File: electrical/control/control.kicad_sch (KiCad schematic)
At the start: 46 parts, among them J1 USB4105-GF-A, J3 SWD, J4 QWIIC, J5 TC2030-NL, J6 UART, SW1 SYS, U1 RP2040, U2 ABPMRRV001PD2A3, U4 W25Q16JVSSIQ, U5 LP5907MFX-3.3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

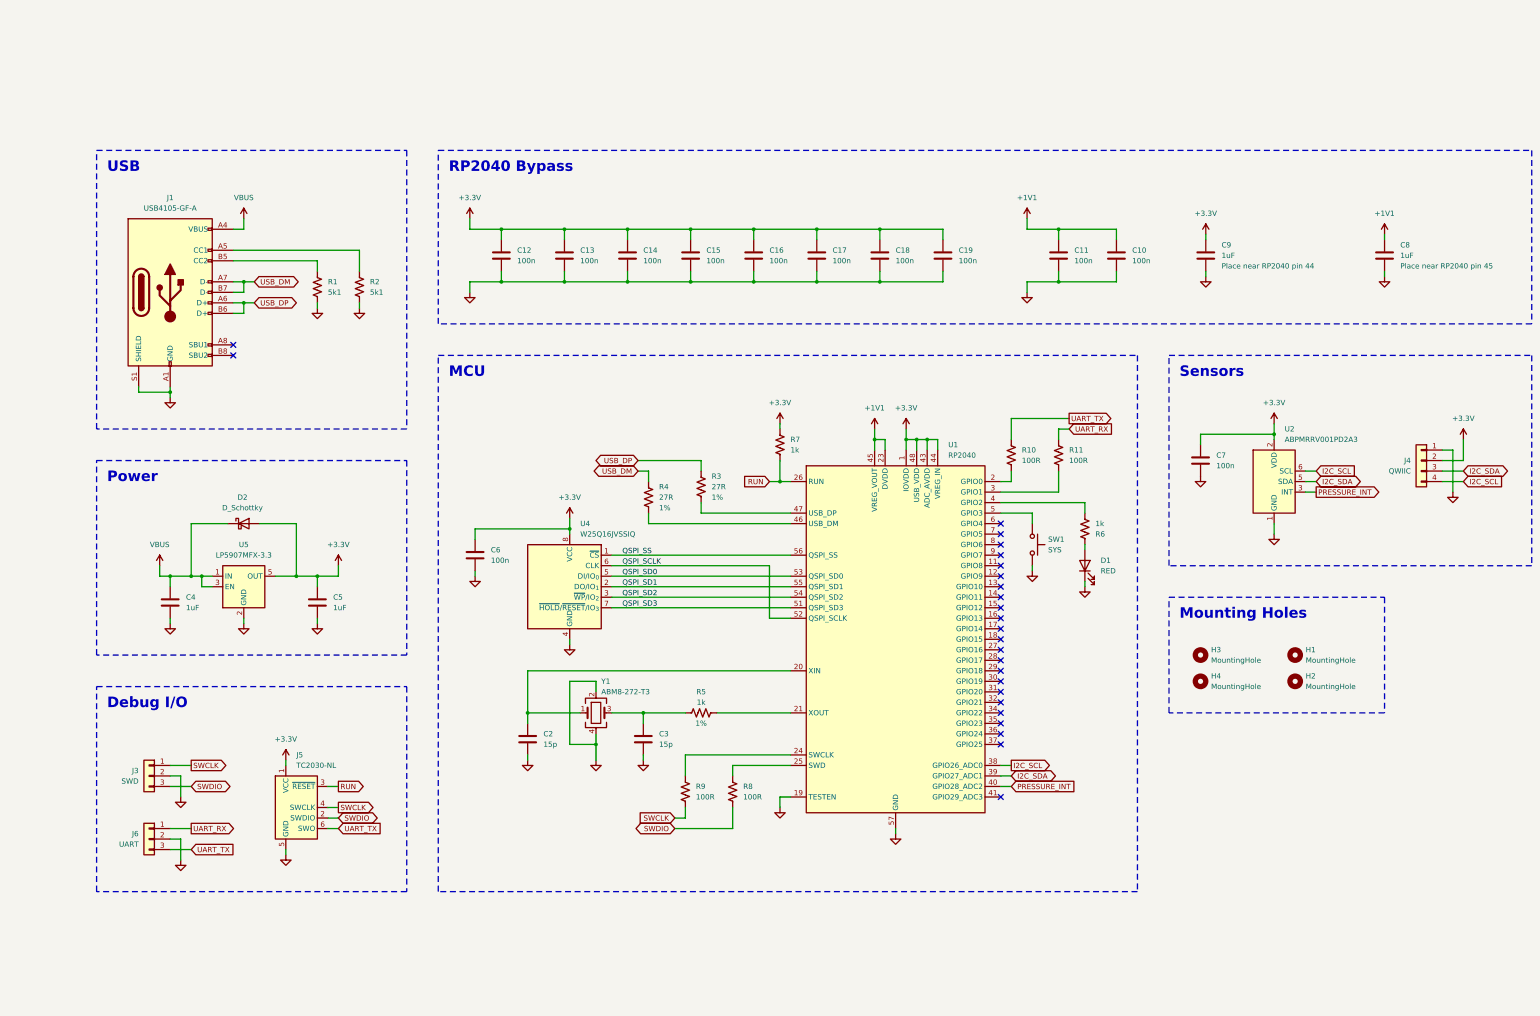
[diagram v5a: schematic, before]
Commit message: Remove diode
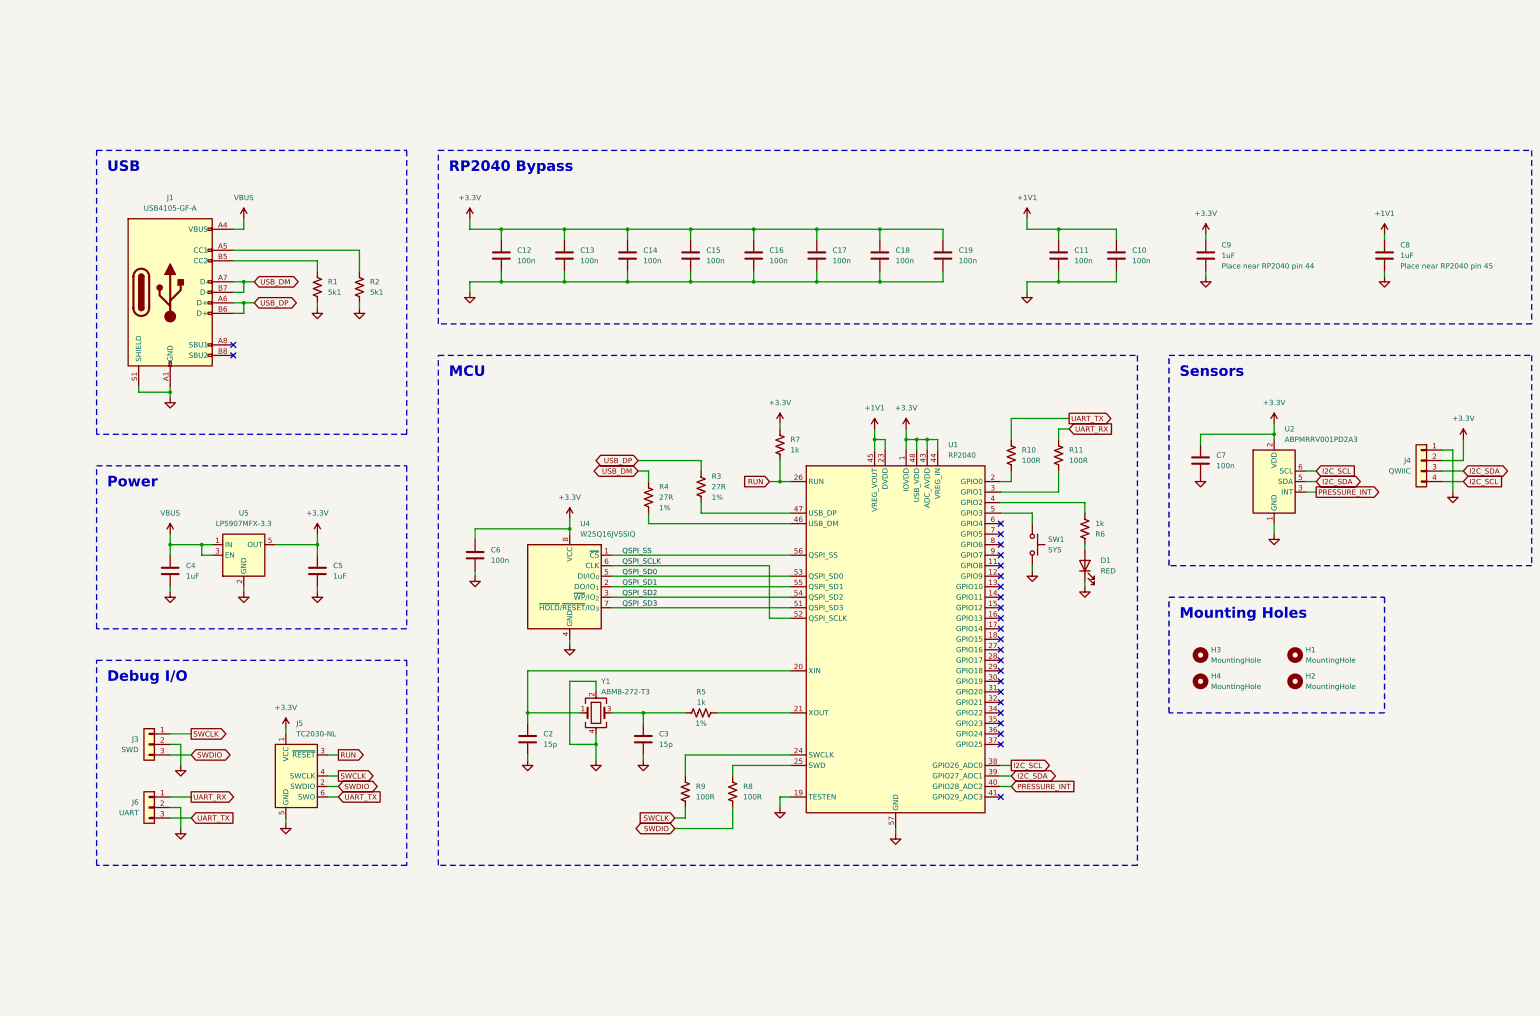
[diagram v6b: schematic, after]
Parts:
- removed D2: D_Schottky, symbol Device:D_Schottky
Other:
- moved on the sheet: C4, C5, J3, J5, J6, U5

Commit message: Reduce number of mounting holes
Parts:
- removed H1, H2, H4: MountingHole, MountingHole:MountingHole_3.2mm_M3, symbol Mechanical:MountingHole
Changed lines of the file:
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@@
 	(rectangle
 		(start 300.99 158.75)
-		(end 353.06 186.69)
+		(end 339.09 180.34)
 		(stroke
 			(width 0)
@@
 	)
 	(symbol
-		(lib_id "Mechanical:MountingHole")
-		(at 331.47 172.72 0)
-		(unit 1)
-		(exclude_from_sim no)
-		(in_bom no)
-		(on_board yes)
-		(dnp no)
-		(fields_autoplaced yes)
-		(property "Reference" "H1"
-			(at 334.01 171.4499 0)
-			(effects
-				(font
-					(size 1.27 1.27)
-				)
-				(justify left)
-			)
-		)
-		(property "Value" "MountingHole"
-			(at 334.01 173.9899 0)
-			(effects
-				(font
-					(size 1.27 1.27)
-				)
-				(justify left)
-			)
-		)
-		(property "Footprint" "MountingHole:MountingHole_3.2mm_M3"
-			(at 331.47 172.72 0)
-			(effects
-				(font
-					(size 1.27 1.27)
-				)
-				(hide yes)
-			)
-		)
-		(property "Datasheet" "~"
-			(at 331.47 172.72 0)
-			(effects
-				(font
-					(size 1.27 1.27)
-				)
-				(hide yes)
-			)
-		)
-		(property "Description" "Mounting Hole without connection"
-			(at 331.47 172.72 0)
-			(effects
-				(font
-					(size 1.27 1.27)
-				)
-				(hide yes)
-			)
-		)
-		(instances
-			(project "control"
-				(path "/da26d94e-7a50-4b99-9678-5aaaf6987a15"
-					(reference "H1")
-					(unit 1)
-				)
-			)
-		)
-	)
-	(symbol
 		(lib_id "Device:R_US")
 		(at 105.41 83.82 0)
@@
 	)
 	(symbol
-		(lib_id "Mechanical:MountingHole")
-		(at 308.61 179.07 0)
-		(unit 1)
-		(exclude_from_sim no)
-		(in_bom no)
-		(on_board yes)
-		(dnp no)
-		(fields_autoplaced yes)
-		(property "Reference" "H4"
-			(at 311.15 177.7999 0)
-			(effects
-				(font
-					(size 1.27 1.27)
-				)
-				(justify left)
-			)
-		)
-		(property "Value" "MountingHole"
-			(at 311.15 180.3399 0)
-			(effects
-				(font
-					(size 1.27 1.27)
-				)
-				(justify left)
-			)
-		)
-		(property "Footprint" "MountingHole:MountingHole_3.2mm_M3"
-			(at 308.61 179.07 0)
-			(effects
-				(font
-					(size 1.27 1.27)
-				)
-				(hide yes)
-			)
-		)
-		(property "Datasheet" "~"
-			(at 308.61 179.07 0)
-			(effects
-				(font
-					(size 1.27 1.27)
-				)
-				(hide yes)
-			)
-		)
-		(property "Description" "Mounting Hole without connection"
-			(at 308.61 179.07 0)
-			(effects
-				(font
-					(size 1.27 1.27)
-				)
-				(hide yes)
-			)
-		)
-		(instances
-			(project "control"
-				(path "/da26d94e-7a50-4b99-9678-5aaaf6987a15"
-					(reference "H4")
-					(unit 1)
-				)
-			)
-		)
-	)
-	(symbol
 		(lib_id "Device:R_US")
 		(at 184.15 205.74 0)
@@
 					(unit 1)
 				)
-			)
-		)
-	)
-	(symbol
-		(lib_id "Mechanical:MountingHole")
-		(at 331.47 179.07 0)
-		(unit 1)
-		(exclude_from_sim no)
-		(in_bom no)
-		(on_board yes)
-		(dnp no)
-		(fields_autoplaced yes)
-		(property "Reference" "H2"
-			(at 334.01 177.7999 0)
-			(effects
-				(font
-					(size 1.27 1.27)
-				)
-				(justify left)
-			)
-		)
-		(property "Value" "MountingHole"
-			(at 334.01 180.3399 0)
-			(effects
-				(font
-					(size 1.27 1.27)
-				)
-				(justify left)
-			)
-		)
-		(property "Footprint" "MountingHole:MountingHole_3.2mm_M3"
-			(at 331.47 179.07 0)
-			(effects
-				(font
-					(size 1.27 1.27)
-				)
-				(hide yes)
-			)
-		)
-		(property "Datasheet" "~"
-			(at 331.47 179.07 0)
-			(effects
-				(font
-					(size 1.27 1.27)
-				)
-				(hide yes)
-			)
-		)
-		(property "Description" "Mounting Hole without connection"
-			(at 331.47 179.07 0)
-			(effects
-				(font
-					(size 1.27 1.27)
-				)
-				(hide yes)
-			)
-		)
-		(instances
-			(project "control"
-				(path "/da26d94e-7a50-4b99-9678-5aaaf6987a15"
-					(reference "H2")
-					(unit 1)
-				)

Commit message: Assign more part numbers and footprints
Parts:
- J1: LCSC (none) -> C3020560
- SW1: footprint (none) -> Button_Switch_SMD:Panasonic_EVQPUL_EVQPUC; LCSC (none) -> C79175
- U5: LCSC (none) -> C80670
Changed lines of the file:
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@@
+			)
+		)
+		(property "LCSC" "C80670"
+			(at 77.47 148.59 0)
+			(effects
+				(font
+					(size 1.27 1.27)
+				)
+				(hide yes)
 			)
 		)
@@
 			)
 		)
-		(property "Footprint" ""
+		(property "Footprint" "Button_Switch_SMD:Panasonic_EVQPUL_EVQPUC"
 			(at 273.05 146.05 0)
 			(effects
@@
 		(property "Description" "Push button switch, generic, two pins"
 			(at 267.97 146.05 0)
+			(effects
+				(font
+					(size 1.27 1.27)
+				)
+				(hide yes)
+			)
+		)
+		(property "LCSC" "C79175"
+			(at 267.97 146.05 90)
 			(effects
 				(font
@@
 			(at 59.69 85.09 0)
 			(effects
+				(font
+					(size 1.27 1.27)
+				)
+				(hide yes)
+			)
+		)
+		(property "LCSC" "C3020560"
+			(at 59.69 85.09 0)
+			(effects
